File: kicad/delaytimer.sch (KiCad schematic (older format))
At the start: 21 parts, among them P1 CONN_01X04, Q1 MMBT3904, Q2 MMBT3904, Q3 MMBT3906, Q4 MMBT3906, Q5 IRLML6344, U1 NE555

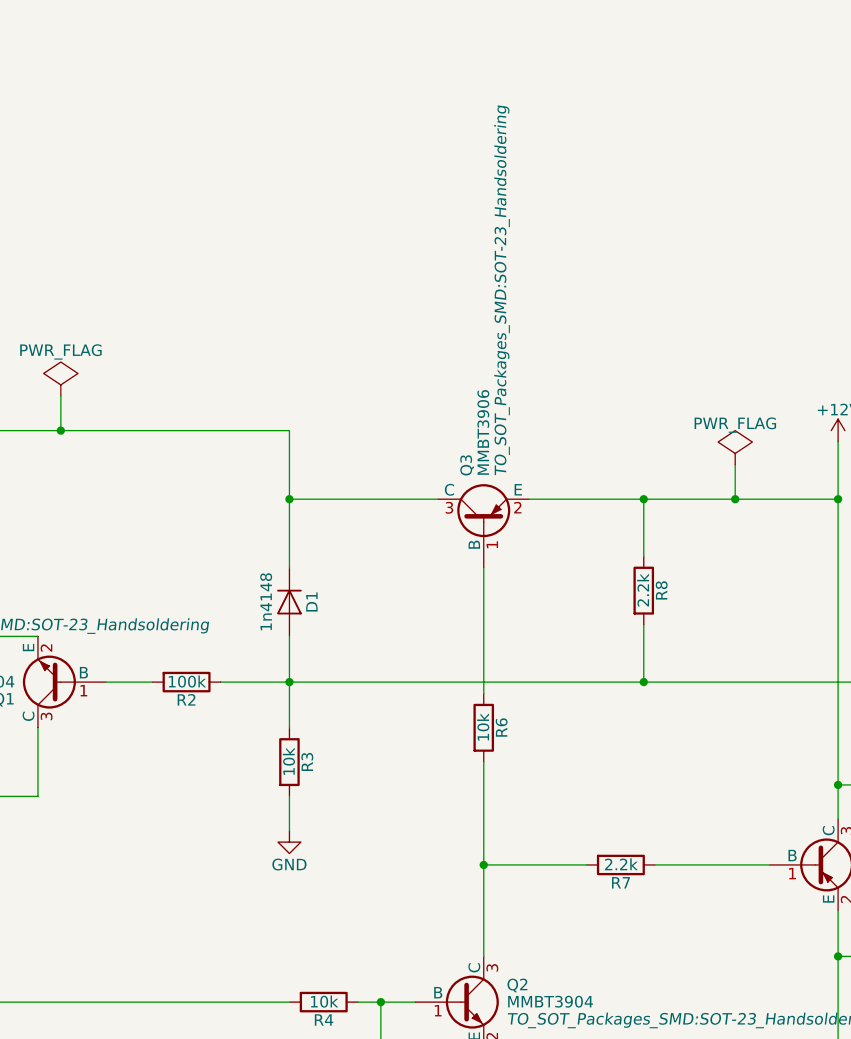
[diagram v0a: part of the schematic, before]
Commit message: Update schema / pcb / readme
- Removed unneeded resistor
- Reduce vias
- Fix labels for header
- Added copper pour on front/back
- UpdatedBOM
- Added Makefile for building BOM CSV
- Update README
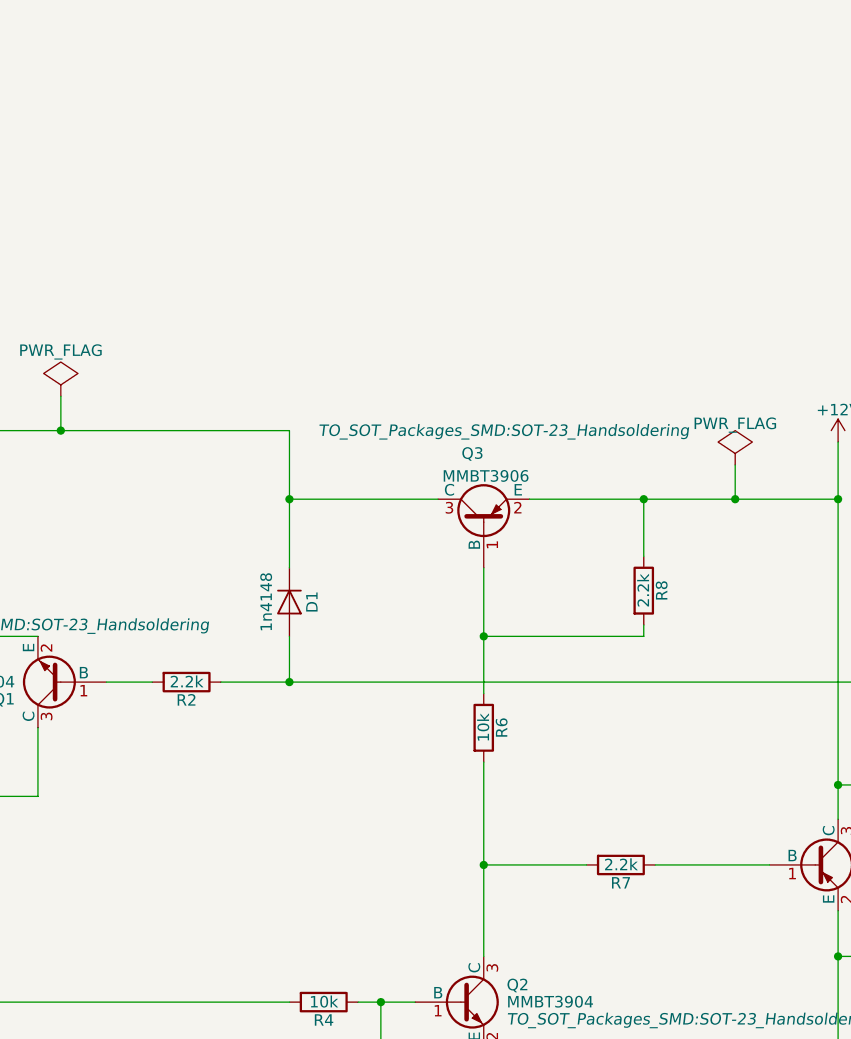
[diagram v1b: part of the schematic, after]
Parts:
- removed R3: 10k, Resistors_SMD:R_0805_HandSoldering, symbol R
- R2: value 100k -> 2.2k
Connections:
- net Switched12V: no longer R8.2
- net at Q3.1 (B), R6.1: now also R8.2
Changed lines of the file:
@@
 U 1 1 58A68A1F
 P 6750 2750
-F 0 "Q3" H 6950 2825 50  0000 L CNN
-F 1 "MMBT3906" H 6950 2750 50  0000 L CNN
-F 2 "TO_SOT_Packages_SMD:SOT-23_Handsoldering" H 6950 2675 50  0000 L CIN
+F 0 "Q3" V 7050 2750 50  0000 L CNN
+F 1 "MMBT3906" V 6950 2550 50  0000 L CNN
+F 2 "TO_SOT_Packages_SMD:SOT-23_Handsoldering" V 7150 1850 50  0000 L CIN
 F 3 "" H 6750 2750 50  0000 L CNN
 	1    6750 2750
@@
 P 5450 3450
 F 0 "R2" V 5530 3450 50  0000 C CNN
-F 1 "100k" V 5450 3450 50  0000 C CNN
+F 1 "2.2k" V 5450 3450 50  0000 C CNN
 F 2 "Resistors_SMD:R_0805_HandSoldering" V 5380 3450 50  0001 C CNN
 F 3 "" H 5450 3450 50  0000 C CNN
@@
 $EndComp
 $Comp
-L R R3
-U 1 1 58A69D3A
-P 5900 3800
-F 0 "R3" V 5980 3800 50  0000 C CNN
-F 1 "10k" V 5900 3800 50  0000 C CNN
-F 2 "Resistors_SMD:R_0805_HandSoldering" V 5830 3800 50  0001 C CNN
-F 3 "" H 5900 3800 50  0000 C CNN
-	1    5900 3800
-	1    0    0    -1
-$EndComp
-$Comp
 L R R8
 U 1 1 58A6A067
@@
 	5600 3450 8650 3450
 Wire Wire Line
-	5900 3250 5900 3650
+	5900 3250 5900 3450
 Connection ~ 5900 3450
 Wire Wire Line
@@
 	7500 4250 8000 4250
 Wire Wire Line
-	7450 3200 7450 3450
-Wire Wire Line
 	6950 2650 8300 2650
 Wire Wire Line
@@
 Wire Wire Line
 	8300 4450 8300 5050
-Connection ~ 7450 3450
 Connection ~ 4100 5450
 Wire Wire Line
@@
 	1    0    0    -1
 $EndComp
-Wire Wire Line
-	5900 3950 5900 4100
-$Comp
-L GND #PWR04
-U 1 1 58A88828
-P 5900 4100
-F 0 "#PWR04" H 5900 3850 50  0001 C CNN
-F 1 "GND" H 5900 3950 50  0000 C CNN
-F 2 "" H 5900 4100 50  0000 C CNN
-F 3 "" H 5900 4100 50  0000 C CNN
-	1    5900 4100
-	1    0    0    -1
-$EndComp
 $Comp
 L +12V #PWR05
@@
 	7850 2500 7850 2650
 Connection ~ 7850 2650
+Wire Wire Line
+	7450 3200 7450 3250
+Wire Wire Line
+	7450 3250 6750 3250
+Connection ~ 6750 3250
 $EndSCHEMATC

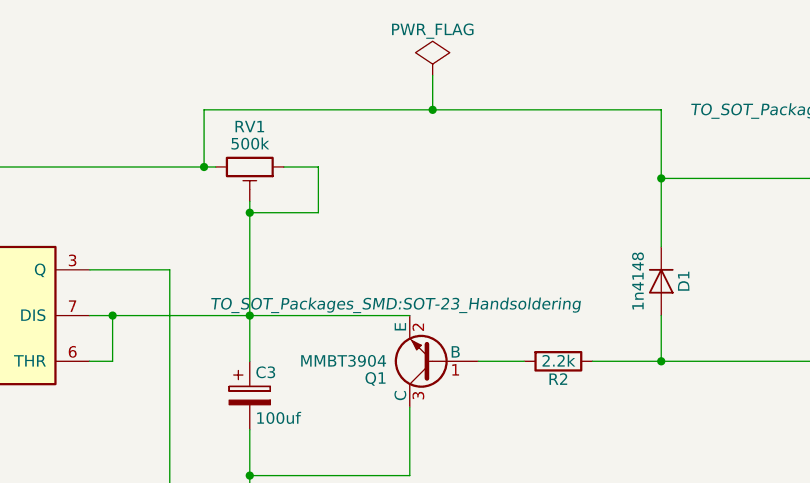
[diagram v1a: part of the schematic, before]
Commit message: Add static resistor option in place of pot
- Added a static resistor (ROpt) so you can save on the price of a pot
- Added measurements to the board for making an enclosure
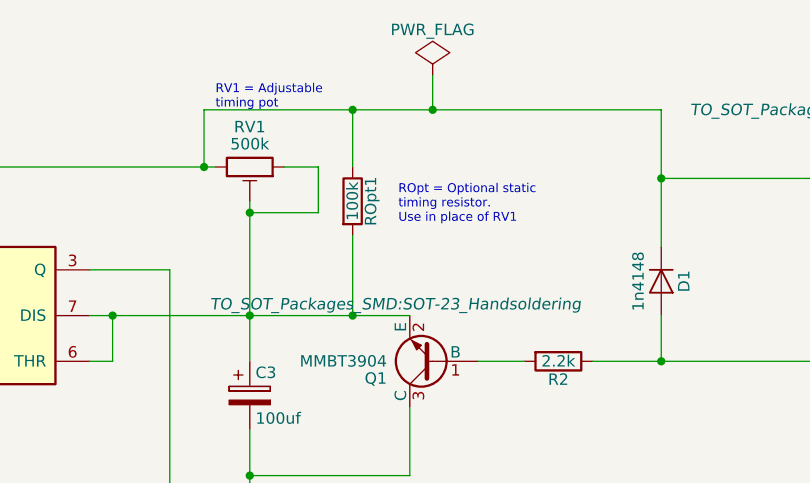
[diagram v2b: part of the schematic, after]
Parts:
- added ROpt1: 100k, Resistors_SMD:R_0805_HandSoldering, symbol R
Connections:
- net VCC: now also ROpt1.1
- net at C3.1, Q1.2 (E), RV1.1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: now also ROpt1.2
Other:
- note added: "ROpt = Optional static \ntiming resistor.\nUse in place of RV1"
- note added: "RV1 = Adjustable\ntiming pot"
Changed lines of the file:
@@
 12VOut
-Wire Wire Line
-	4250 2600 4400 2600
 Wire Wire Line
 	4400 2600 4400 2800
@@
 $EndComp
 $Comp
-L +12V #PWR05
+L +12V #PWR04
 U 1 1 58A88A5B
 P 4350 6150
-F 0 "#PWR05" H 4350 6000 50  0001 C CNN
+F 0 "#PWR04" H 4350 6000 50  0001 C CNN
 F 1 "+12V" H 4350 6290 50  0000 C CNN
 F 2 "" H 4350 6150 50  0000 C CNN
@@
 	4350 6250 4350 6150
 $Comp
-L PWR_FLAG #FLG06
+L PWR_FLAG #FLG05
 U 1 1 58A88E89
 P 4900 2200
-F 0 "#FLG06" H 4900 2295 50  0001 C CNN
+F 0 "#FLG05" H 4900 2295 50  0001 C CNN
 F 1 "PWR_FLAG" H 4900 2400 50  0000 C CNN
 F 2 "" H 4900 2200 50  0000 C CNN
@@
 Connection ~ 4900 2350
 $Comp
-L PWR_FLAG #FLG07
+L PWR_FLAG #FLG06
 U 1 1 58A89467
 P 3350 5350
-F 0 "#FLG07" H 3350 5445 50  0001 C CNN
+F 0 "#FLG06" H 3350 5445 50  0001 C CNN
 F 1 "PWR_FLAG" H 3350 5530 50  0000 C CNN
 F 2 "" H 3350 5350 50  0000 C CNN
@@
 Connection ~ 3350 5450
 $Comp
-L PWR_FLAG #FLG08
+L PWR_FLAG #FLG07
 U 1 1 58A896CC
 P 7850 2500
-F 0 "#FLG08" H 7850 2595 50  0001 C CNN
+F 0 "#FLG07" H 7850 2595 50  0001 C CNN
 F 1 "PWR_FLAG" H 7850 2680 50  0000 C CNN
 F 2 "" H 7850 2500 50  0000 C CNN
@@
 	7450 3250 6750 3250
 Connection ~ 6750 3250
+$Comp
+L R ROpt1
+U 1 1 58AA75F7
+P 4550 2750
+F 0 "ROpt1" V 4630 2750 50  0000 C CNN
+F 1 "100k" V 4550 2750 50  0000 C CNN
+F 2 "Resistors_SMD:R_0805_HandSoldering" V 4480 2750 50  0001 C CNN
+F 3 "" H 4550 2750 50  0000 C CNN
+	1    4550 2750
+	1    0    0    -1
+$EndComp
+Connection ~ 4550 3250
+Wire Wire Line
+	4550 2900 4550 3250
+Wire Wire Line
+	4550 2600 4550 2350
+Connection ~ 4550 2350
+Wire Wire Line
+	4250 2600 4400 2600
+Text Notes 4750 2850 0    39   ~ 0
+ROpt = Optional static \ntiming resistor.\nUse in place of RV1
+Text Notes 3950 2350 0    39   ~ 0
+RV1 = Adjustable\ntiming pot
 $EndSCHEMATC

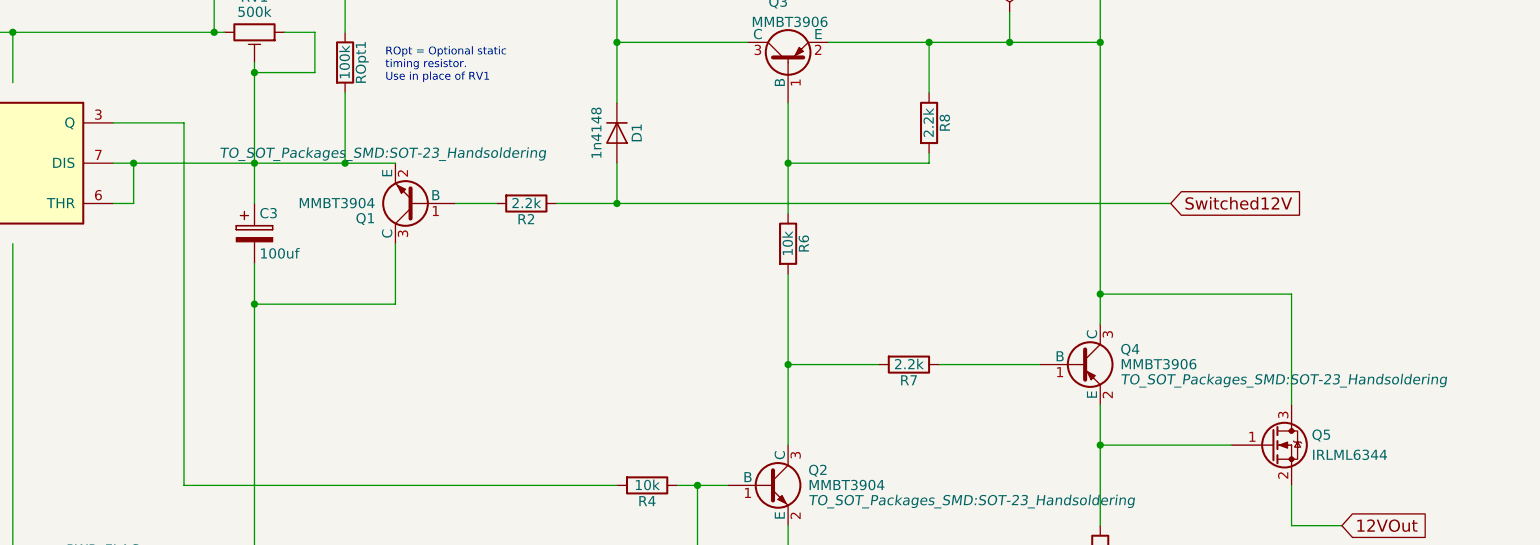
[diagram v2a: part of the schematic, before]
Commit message: Update to v1.1
- Fix Q1,Q4 which were connected wrong
- Fix routing of GND to use GND plane
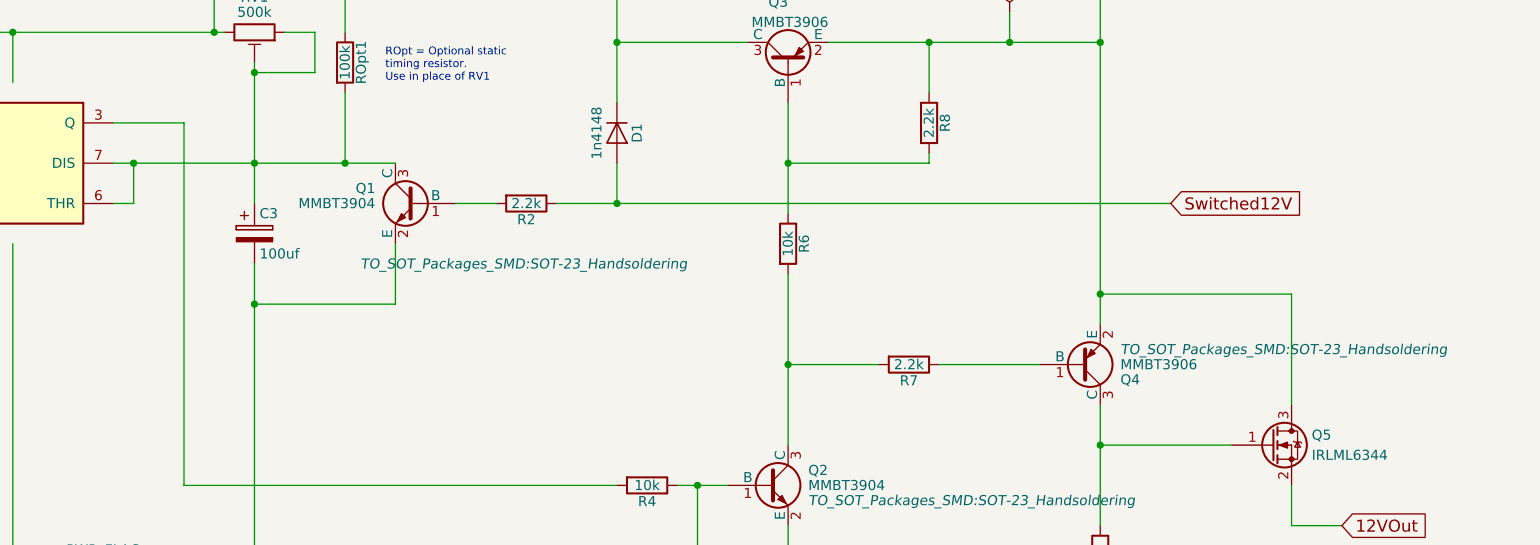
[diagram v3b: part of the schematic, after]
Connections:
- net +12V: now also Q4.2 (E); no longer Q4.3 (C)
- net GND: now also Q1.2 (E); no longer Q1.3 (C)
- net at C3.1, ROpt1.2, RV1.1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: now also Q1.3 (C); no longer Q1.2 (E)
- net at Q5.1 (G), R9.1: now also Q4.3 (C); no longer Q4.2 (E)
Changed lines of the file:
@@
 Sheet 1 1
 Title "Adjustable Delay Timer"
-Date "2017-02-18"
-Rev "v1.0"
+Date "2017-03-05"
+Rev "v1.1"
 Comp "Aaron Turner <synfinatic@gmail.com>"
 Comment1 "https://synfin.net/delaytimer"
@@
 F 3 "" H 8200 4250 50  0000 L CNN
 	1    8200 4250
-	1    0    0    -1
+	1    0    0    1
 $EndComp
 $Comp
@@
 F 0 "Q1" H 5100 3525 50  0000 L CNN
 F 1 "MMBT3904" H 5100 3450 50  0000 L CNN
-F 2 "TO_SOT_Packages_SMD:SOT-23_Handsoldering" H 4250 3200 50  0000 L CIN
+F 2 "TO_SOT_Packages_SMD:SOT-23_Handsoldering" H 3550 3150 50  0000 L CIN
 F 3 "" H 4900 3450 50  0000 L CNN
 	1    4900 3450
-	-1   0    0    1
+	-1   0    0    -1
 $EndComp
 $Comp
